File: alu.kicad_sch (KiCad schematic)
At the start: 41 parts, among them J0 640-USB4970-00-A, SW0 418127270904, SW1 418127270904, SW2 418127270904, U0 SN74LS08N, U1 SN74HC86N, U2 SN74HC86N, U3 SN74LS08N, U4 SN74LS08N, U5 CD74HCT32E

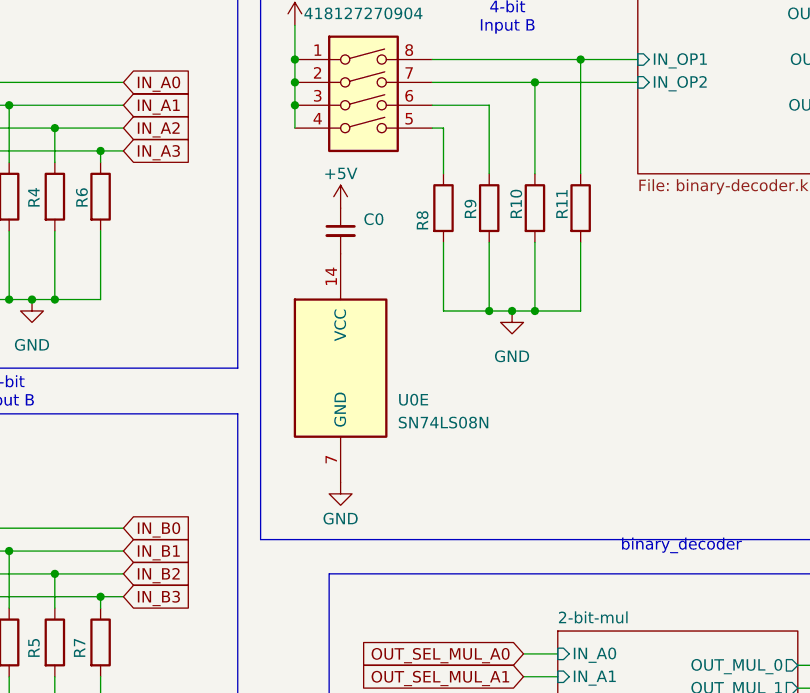
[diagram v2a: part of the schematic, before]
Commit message: feat: pcb layout position
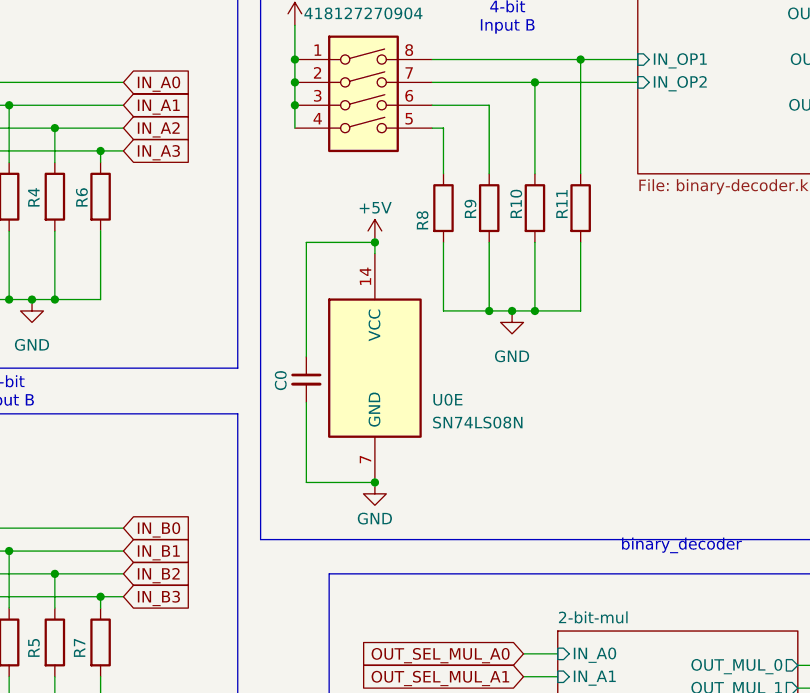
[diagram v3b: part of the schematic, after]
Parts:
- R0, R1, R10, R11, R2, R3, R4, R5, R6, R7, R8, R9: value RC0603FR-07220RL -> CRG0603J10K - 3399584; footprint Resistor_SMD:R_2512_6332Metric_Pad1.40x3.35mm_HandSolder -> Resistor_SMD:R_0603_1608Metric_Pad0.98x0.95mm_HandSolder
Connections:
- net +5V: now also U0.14 (VCC)
- net GND: now also C0.2
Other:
- moved on the sheet: C0, U0E
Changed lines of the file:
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@@
 	)
 	(junction
+		(at 87.63 74.93)
+		(diameter 0)
+		(color 0 0 0 0)
+	)
+	(junction
 		(at 128.27 161.29)
 		(diameter 0)
@@
 	)
 	(junction
+		(at 87.63 48.26)
+		(diameter 0)
+		(color 0 0 0 0)
+	)
+	(junction
 		(at 52.07 104.14)
 		(diameter 0)
@@
 	(wire
 		(pts
+			(xy 80.01 66.04) (xy 80.01 74.93)
+		)
+		(stroke
+			(width 0)
+			(type default)
+		)
+	)
+	(wire
+		(pts
 			(xy 29.21 147.32) (xy 31.75 147.32)
 		)
@@
 	(wire
 		(pts
+			(xy 80.01 60.96) (xy 80.01 48.26)
+		)
+		(stroke
+			(width 0)
+			(type default)
+		)
+	)
+	(wire
+		(pts
 			(xy 59.69 132.08) (xy 62.23 132.08)
 		)
@@
 	(wire
 		(pts
+			(xy 87.63 48.26) (xy 87.63 49.53)
+		)
+		(stroke
+			(width 0)
+			(type default)
+		)
+	)
+	(wire
+		(pts
 			(xy 52.07 104.14) (xy 49.53 104.14)
 		)
@@
 	(wire
 		(pts
+			(xy 80.01 74.93) (xy 87.63 74.93)
+		)
+		(stroke
+			(width 0)
+			(type default)
+		)
+	)
+	(wire
+		(pts
 			(xy 25.4 33.02) (xy 25.4 35.56)
 		)
@@
 	(wire
 		(pts
+			(xy 80.01 48.26) (xy 87.63 48.26)
+		)
+		(stroke
+			(width 0)
+			(type default)
+		)
+	)
+	(wire
+		(pts
 			(xy 25.4 25.4) (xy 25.4 30.48)
 		)
@@
 			)
 		)
-		(property "Value" "RC0603FR-07220RL"
+		(property "Value" "CRG0603J10K - 3399584"
 			(at 102.87 45.7199 0)
 			(hide yes)
@@
 			)
 		)
-		(property "Footprint" "Resistor_SMD:R_2512_6332Metric_Pad1.40x3.35mm_HandSolder"
+		(property "Footprint" "Resistor_SMD:R_0603_1608Metric_Pad0.98x0.95mm_HandSolder"
 			(at 98.552 44.45 90)
 			(hide yes)
@@
 			)
 		)
-		(property "Value" "RC0603FR-07220RL"
+		(property "Value" "CRG0603J10K - 3399584"
 			(at 113.03 45.7199 0)
 			(hide yes)
@@
 			)
 		)
-		(property "Footprint" "Resistor_SMD:R_2512_6332Metric_Pad1.40x3.35mm_HandSolder"
+		(property "Footprint" "Resistor_SMD:R_0603_1608Metric_Pad0.98x0.95mm_HandSolder"
 			(at 108.712 44.45 90)
 			(hide yes)
@@
 	(symbol
 		(lib_id "power:GND")
-		(at 83.82 74.93 0)
+		(at 87.63 74.93 0)
 		(unit 1)
 		(body_style 1)
@@
 		(dnp no)
 		(property "Reference" "#PWR06"
-			(at 83.82 81.28 0)
+			(at 87.63 81.28 0)
 			(hide yes)
 			(show_name no)
@@
 		)
 		(property "Value" "GND"
-			(at 83.82 78.994 0)
+			(at 87.63 78.994 0)
 			(show_name no)
 			(do_not_autoplace no)
@@
 		)
 		(property "Footprint" ""
-			(at 83.82 74.93 0)
+			(at 87.63 74.93 0)
 			(hide yes)
 			(show_name no)
@@
 		)
 		(property "Datasheet" ""
-			(at 83.82 74.93 0)
+			(at 87.63 74.93 0)
 			(hide yes)
 			(show_name no)
@@
 		)
 		(property "Description" "Power symbol creates a global label with name \"GND\" , ground"
-			(at 83.82 74.93 0)
+			(at 87.63 74.93 0)
 			(hide yes)
 			(show_name no)
@@
 			)
 		)
-		(property "Value" "RC0603FR-07220RL"
+		(property "Value" "CRG0603J10K - 3399584"
 			(at 44.45 44.4499 0)
 			(hide yes)
@@
 			)
 		)
-		(property "Footprint" "Resistor_SMD:R_2512_6332Metric_Pad1.40x3.35mm_HandSolder"
+		(property "Footprint" "Resistor_SMD:R_0603_1608Metric_Pad0.98x0.95mm_HandSolder"
 			(at 40.132 43.18 90)
 			(hide yes)
@@
 			)
 		)
-		(property "Value" "RC0603FR-07220RL"
+		(property "Value" "CRG0603J10K - 3399584"
 			(at 107.95 45.7199 0)
 			(hide yes)
@@
 			)
 		)
-		(property "Footprint" "Resistor_SMD:R_2512_6332Metric_Pad1.40x3.35mm_HandSolder"
+		(property "Footprint" "Resistor_SMD:R_0603_1608Metric_Pad0.98x0.95mm_HandSolder"
 			(at 103.632 44.45 90)
 			(hide yes)
@@
 			)
 		)
-		(property "Value" "RC0603FR-07220RL"
+		(property "Value" "CRG0603J10K - 3399584"
 			(at 59.69 44.4499 0)
 			(hide yes)
@@
 			)
 		)
-		(property "Footprint" "Resistor_SMD:R_2512_6332Metric_Pad1.40x3.35mm_HandSolder"
+		(property "Footprint" "Resistor_SMD:R_0603_1608Metric_Pad0.98x0.95mm_HandSolder"
 			(at 55.372 43.18 90)
 			(hide yes)
@@
 			)
 		)
-		(property "Value" "RC0603FR-07220RL"
+		(property "Value" "CRG0603J10K - 3399584"
 			(at 49.53 93.9799 0)
 			(hide yes)
@@
 			)
 		)
-		(property "Footprint" "Resistor_SMD:R_2512_6332Metric_Pad1.40x3.35mm_HandSolder"
+		(property "Footprint" "Resistor_SMD:R_0603_1608Metric_Pad0.98x0.95mm_HandSolder"
 			(at 45.212 92.71 90)
 			(hide yes)
@@
 			)
 		)
-		(property "Value" "RC0603FR-07220RL"
+		(property "Value" "CRG0603J10K - 3399584"
 			(at 54.61 44.4499 0)
 			(hide yes)
@@
 			)
 		)
-		(property "Footprint" "Resistor_SMD:R_2512_6332Metric_Pad1.40x3.35mm_HandSolder"
+		(property "Footprint" "Resistor_SMD:R_0603_1608Metric_Pad0.98x0.95mm_HandSolder"
 			(at 50.292 43.18 90)
 			(hide yes)
@@
 			)
 		)
-		(property "Value" "RC0603FR-07220RL"
+		(property "Value" "CRG0603J10K - 3399584"
 			(at 59.69 93.9799 0)
 			(hide yes)
@@
 			)
 		)
-		(property "Footprint" "Resistor_SMD:R_2512_6332Metric_Pad1.40x3.35mm_HandSolder"
+		(property "Footprint" "Resistor_SMD:R_0603_1608Metric_Pad0.98x0.95mm_HandSolder"
 			(at 55.372 92.71 90)
 			(hide yes)
@@
 	(symbol
 		(lib_id "74xx:74LS08")
-		(at 83.82 62.23 0)
+		(at 87.63 62.23 0)
 		(unit 5)
 		(body_style 1)
@@
 		(dnp no)
 		(property "Reference" "U0"
-			(at 90.17 65.786 0)
+			(at 93.98 65.786 0)
 			(show_name no)
 			(do_not_autoplace no)
@@
 		)
 		(property "Value" "SN74LS08N"
-			(at 90.17 68.326 0)
+			(at 93.98 68.326 0)
 			(show_name no)
 			(do_not_autoplace no)
@@
 		)
 		(property "Footprint" "Package_DIP:DIP-14_W7.62mm_LongPads"
-			(at 83.82 62.23 0)
+			(at 87.63 62.23 0)
 			(hide yes)
 			(show_name no)
@@
 		)
 		(property "Datasheet" "https://www.ti.com/lit/ds/symlink/sn74hc86.pdf"
-			(at 83.82 62.23 0)
+			(at 87.63 62.23 0)
 			(hide yes)
 			(show_name no)
@@
 		)
 		(property "Description" "Quad And2"
-			(at 83.82 62.23 0)
+			(at 87.63 62.23 0)
 			(hide yes)
 			(show_name no)
@@
 	(symbol
 		(lib_id "power:+5V")
-		(at 83.82 44.45 0)
+		(at 87.63 48.26 0)
 		(unit 1)
 		(body_style 1)
@@
 		(dnp no)
 		(property "Reference" "#PWR05"
-			(at 83.82 48.26 0)
+			(at 87.63 52.07 0)
 			(hide yes)
 			(show_name no)
@@
 		)
 		(property "Value" "+5V"
-			(at 83.82 40.64 0)
+			(at 87.63 44.45 0)
 			(show_name no)
 			(do_not_autoplace no)
@@
 		)
 		(property "Footprint" ""
-			(at 83.82 44.45 0)
+			(at 87.63 48.26 0)
 			(hide yes)
 			(show_name no)
@@
 		)
 		(property "Datasheet" ""
-			(at 83.82 44.45 0)
+			(at 87.63 48.26 0)
 			(hide yes)
 			(show_name no)
@@
 		)
 		(property "Description" "Power symbol creates a global label with name \"+5V\""
-			(at 83.82 44.45 0)
+			(at 87.63 48.26 0)
 			(hide yes)
 			(show_name no)
@@
 			)
 		)
-		(property "Value" "RC0603FR-07220RL"
+		(property "Value" "CRG0603J10K - 3399584"
 			(at 49.53 44.4499 0)
 			(hide yes)
@@
 			)
 		)
-		(property "Footprint" "Resistor_SMD:R_2512_6332Metric_Pad1.40x3.35mm_HandSolder"
+		(property "Footprint" "Resistor_SMD:R_0603_1608Metric_Pad0.98x0.95mm_HandSolder"
 			(at 45.212 43.18 90)
 			(hide yes)
@@
 	(symbol
 		(lib_id "Device:C_Small")
-		(at 83.82 46.99 0)
+		(at 80.01 63.5 0)
 		(unit 1)
 		(body_style 1)
@@
 		(in_pos_files yes)
 		(dnp no)
-		(fields_autoplaced yes)
 		(property "Reference" "C0"
-			(at 86.36 45.7262 0)
+			(at 77.216 64.77 90)
 			(show_name no)
 			(do_not_autoplace no)
@@
 		)
 		(property "Value" "CC0603KRX7R9BB104"
-			(at 86.36 48.2662 0)
+			(at 82.55 64.7762 0)
 			(hide yes)
 			(show_name no)
@@
 		)
 		(property "Footprint" "Capacitor_SMD:C_0603_1608Metric_Pad1.08x0.95mm_HandSolder"
-			(at 83.82 46.99 0)
+			(at 80.01 63.5 0)
 			(hide yes)
 			(show_name no)
@@
 		)
 		(property "Datasheet" ""
-			(at 83.82 46.99 0)
+			(at 80.01 63.5 0)
 			(hide yes)
 			(show_name no)
@@
 		)
 		(property "Description" "Unpolarized capacitor, small symbol"
-			(at 83.82 46.99 0)
+			(at 80.01 63.5 0)
 			(hide yes)
 			(show_name no)
@@
 			)
 		)
-		(property "Value" "RC0603FR-07220RL"
+		(property "Value" "CRG0603J10K - 3399584"
 			(at 54.61 93.9799 0)
 			(hide yes)
@@
 			)
 		)
-		(property "Footprint" "Resistor_SMD:R_2512_6332Metric_Pad1.40x3.35mm_HandSolder"
+		(property "Footprint" "Resistor_SMD:R_0603_1608Metric_Pad0.98x0.95mm_HandSolder"
 			(at 50.292 92.71 90)
 			(hide yes)
@@
 			)
 		)
-		(property "Value" "RC0603FR-07220RL"
+		(property "Value" "CRG0603J10K - 3399584"
 			(at 44.45 93.9799 0)
 			(hide yes)
@@
 			)
 		)
-		(property "Footprint" "Resistor_SMD:R_2512_6332Metric_Pad1.40x3.35mm_HandSolder"
+		(property "Footprint" "Resistor_SMD:R_0603_1608Metric_Pad0.98x0.95mm_HandSolder"
 			(at 40.132 92.71 90)
 			(hide yes)
@@
 			)
 		)
-		(property "Value" "RC0603FR-07220RL"
+		(property "Value" "CRG0603J10K - 3399584"
 			(at 97.79 45.7199 0)
 			(hide yes)
@@
 			)
 		)
-		(property "Footprint" "Resistor_SMD:R_2512_6332Metric_Pad1.40x3.35mm_HandSolder"
+		(property "Footprint" "Resistor_SMD:R_0603_1608Metric_Pad0.98x0.95mm_HandSolder"
 			(at 93.472 44.45 90)
 			(hide yes)

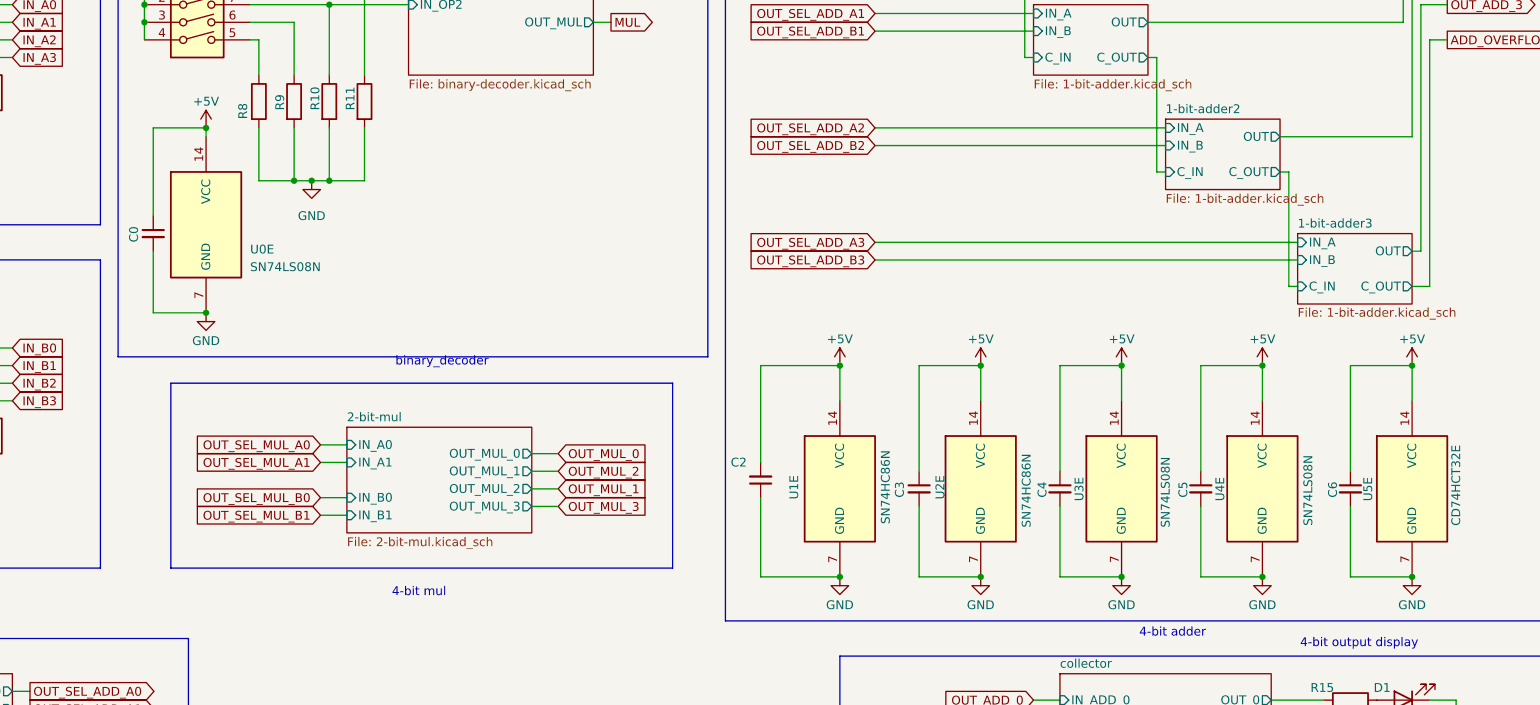
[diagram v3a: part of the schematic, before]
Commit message: Remove capacitors + change R and C footprints + finish PCB routing
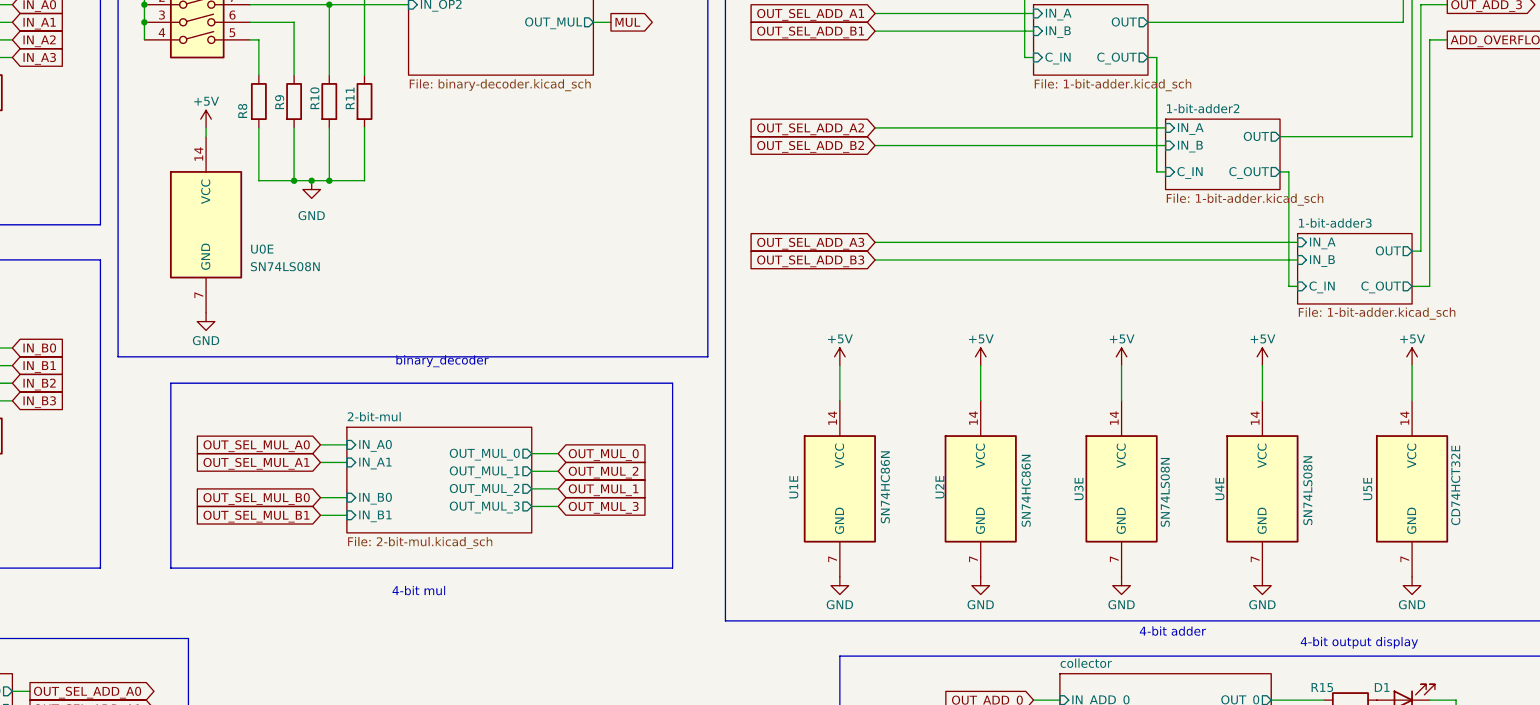
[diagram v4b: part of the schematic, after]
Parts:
- removed C0, C2, C3, C4, C5, C6: CC0603KRX7R9BB104, Capacitor_SMD:C_0603_1608Metric_Pad1.08x0.95mm_HandSolder, symbol Device:C_Small
- C1: footprint Capacitor_SMD:C_0201_0603Metric_Pad0.64x0.40mm_HandSolder -> Capacitor_SMD:C_0603_1608Metric_Pad1.08x0.95mm_HandSolder
- R12, R13: footprint Resistor_SMD:R_0201_0603Metric_Pad0.64x0.40mm_HandSolder -> Resistor_SMD:R_0603_1608Metric_Pad0.98x0.95mm_HandSolder
- R14, R15, R16, R17, R18: footprint Resistor_SMD:R_2512_6332Metric_Pad1.40x3.35mm_HandSolder -> Resistor_SMD:R_0603_1608Metric_Pad0.98x0.95mm_HandSolder

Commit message: fix: reput capas -- where is my gift?
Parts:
- added C0, C2, C3, C4, C5, C6: C_Small, Capacitor_SMD:C_0603_1608Metric, symbol Device:C_Small
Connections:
- net +5V: now also C0.1, C2.1, C3.1, C4.1, C5.1, C6.1
- net GND: now also C0.2, C2.2, C3.2, C4.2, C5.2, C6.2
- no-connect marks 0 -> 1

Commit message: feat: missing pull up
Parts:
- R0, R1, R10, R11, R2, R3, R4, R5, R6, R7, R8, R9: value CRG0603J10K - 3399584 -> 10k
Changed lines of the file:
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@@
 			)
 		)
-		(property "Value" "CRG0603J10K - 3399584"
+		(property "Value" "10k"
 			(at 102.87 45.7199 0)
 			(effects
@@
 			)
 		)
-		(property "Value" "CRG0603J10K - 3399584"
+		(property "Value" "10k"
 			(at 113.03 45.7199 0)
 			(effects
@@
 			)
 		)
-		(property "Value" "CRG0603J10K - 3399584"
+		(property "Value" "10k"
 			(at 44.45 44.4499 0)
 			(effects
@@
 			)
 		)
-		(property "Value" "CRG0603J10K - 3399584"
+		(property "Value" "10k"
 			(at 107.95 45.7199 0)
 			(effects
@@
 			)
 		)
-		(property "Value" "CRG0603J10K - 3399584"
+		(property "Value" "10k"
 			(at 59.69 44.4499 0)
 			(effects
@@
 			)
 		)
-		(property "Value" "CRG0603J10K - 3399584"
+		(property "Value" "10k"
 			(at 49.53 93.9799 0)
 			(effects
@@
 			)
 		)
-		(property "Value" "CRG0603J10K - 3399584"
+		(property "Value" "10k"
 			(at 54.61 44.4499 0)
 			(effects
@@
 			)
 		)
-		(property "Value" "CRG0603J10K - 3399584"
+		(property "Value" "10k"
 			(at 59.69 93.9799 0)
 			(effects
@@
 			)
 		)
-		(property "Value" "CRG0603J10K - 3399584"
+		(property "Value" "10k"
 			(at 49.53 44.4499 0)
 			(effects
@@
 			)
 		)
-		(property "Value" "CRG0603J10K - 3399584"
+		(property "Value" "10k"
 			(at 54.61 93.9799 0)
 			(effects
@@
 			)
 		)
-		(property "Value" "CRG0603J10K - 3399584"
+		(property "Value" "10k"
 			(at 44.45 93.9799 0)
 			(effects
@@
 			)
 		)
-		(property "Value" "CRG0603J10K - 3399584"
+		(property "Value" "10k"
 			(at 97.79 45.7199 0)
 			(effects

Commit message: feat: multiplier schema
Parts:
- R0, R1, R10, R11, R2, R3, R4, R5, R6, R7, R8, R9: value 10k -> CRG0603J10K - 3399584
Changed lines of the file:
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@@
 			)
 		)
-		(property "Value" "10k"
+		(property "Value" "CRG0603J10K - 3399584"
 			(at 102.87 45.7199 0)
 			(effects
@@
 			)
 		)
-		(property "Value" "10k"
+		(property "Value" "CRG0603J10K - 3399584"
 			(at 113.03 45.7199 0)
 			(effects
@@
 			)
 		)
-		(property "Value" "10k"
+		(property "Value" "CRG0603J10K - 3399584"
 			(at 44.45 44.4499 0)
 			(effects
@@
 			)
 		)
-		(property "Value" "10k"
+		(property "Value" "CRG0603J10K - 3399584"
 			(at 107.95 45.7199 0)
 			(effects
@@
 			)
 		)
-		(property "Value" "10k"
+		(property "Value" "CRG0603J10K - 3399584"
 			(at 59.69 44.4499 0)
 			(effects
@@
 			)
 		)
-		(property "Value" "10k"
+		(property "Value" "CRG0603J10K - 3399584"
 			(at 49.53 93.9799 0)
 			(effects
@@
 			)
 		)
-		(property "Value" "10k"
+		(property "Value" "CRG0603J10K - 3399584"
 			(at 54.61 44.4499 0)
 			(effects
@@
 			)
 		)
-		(property "Value" "10k"
+		(property "Value" "CRG0603J10K - 3399584"
 			(at 59.69 93.9799 0)
 			(effects
@@
 			)
 		)
-		(property "Value" "10k"
+		(property "Value" "CRG0603J10K - 3399584"
 			(at 49.53 44.4499 0)
 			(effects
@@
 			)
 		)
-		(property "Value" "10k"
+		(property "Value" "CRG0603J10K - 3399584"
 			(at 54.61 93.9799 0)
 			(effects
@@
 			)
 		)
-		(property "Value" "10k"
+		(property "Value" "CRG0603J10K - 3399584"
 			(at 44.45 93.9799 0)
 			(effects
@@
 			)
 		)
-		(property "Value" "10k"
+		(property "Value" "CRG0603J10K - 3399584"
 			(at 97.79 45.7199 0)
 			(effects
